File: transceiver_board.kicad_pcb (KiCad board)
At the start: 2 copper layers, 126 parts, among them J1 85505-5113, J2 Conn_01x01_Male, J3 SMA_Connector, J4 Conn_01x01_Male, J5 SMA_Connector, Q1 BC547, Q2 BC547, T1 S558-5999-46-F, U1 LAN83C185-JT, U2 ltc6752ims8-2-pbf, U4 AP63203WU, U5 AP63205WU, U6 LM317_TO-220, U7 LM317_TO-220, Y1 25 MHz

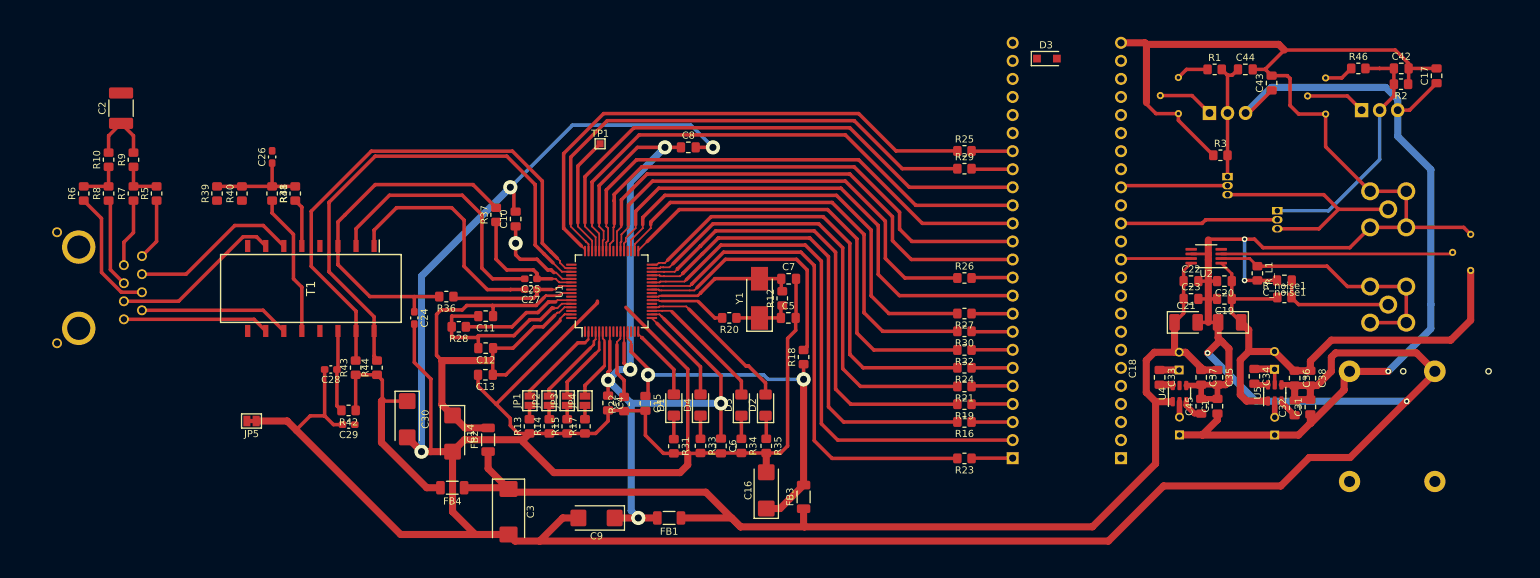
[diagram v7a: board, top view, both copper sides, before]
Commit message: tweaked power circuit, sorted drc errors and warnings, visual checked pcb
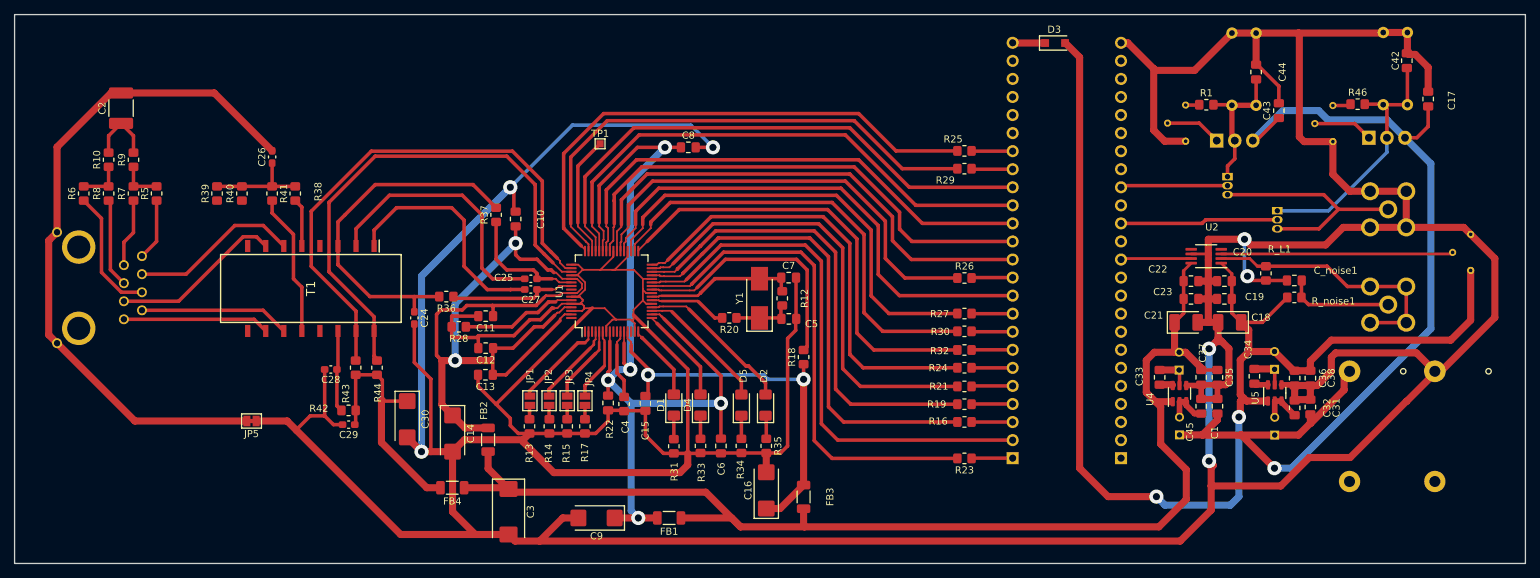
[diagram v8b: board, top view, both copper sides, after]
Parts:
- added R11: 240R, Resistor_THT:R_Axial_DIN0207_L6.3mm_D2.5mm_P10.16mm_Horizontal, B.Cu at (187.6, 43.8)
- added R4: 240R, Resistor_THT:R_Axial_DIN0207_L6.3mm_D2.5mm_P10.16mm_Horizontal, B.Cu at (212.3, 43.7)
- J3: value SMA_Connector -> Laser
- J5: value SMA_Connector -> Receiver Connector
- R1, R46: value 160 -> 180R
- R2, R3: value 120 -> 240R; footprint Resistor_SMD:R_0805_2012Metric_Pad1.20x1.40mm_HandSolder -> Resistor_THT:R_Axial_DIN0207_L6.3mm_D2.5mm_P10.16mm_Horizontal; moved to B.Cu
- moved R3 17.9 mm to (191.0, 43.8), turned to -90 degrees
- moved R2 7.69 mm to (208.9, 43.7), turned to -90 degrees
- moved R1 5.11 mm to (184.0, 53.9)
- moved R46 5.03 mm to (205.3, 53.8)
- moved C43 4.01 mm to (194.2, 54.7)
- moved RV3 4.01 mm to (181.1, 59.0)
- moved RV2 4.01 mm to (201.8, 59.1)
- moved U6 4.01 mm to (206.9, 58.5)
- moved U7 4.01 mm to (185.5, 58.9)
- moved C17 3.47 mm to (215.2, 53.1)
- moved D3 2.47 mm to (162.8, 45.2)
- moved C44 1.56 mm to (191.0, 49.3), turned to 90 degrees
- moved C_noise1 1.40 mm to (196.4, 78.6)
- moved R_noise1 1.40 mm to (196.4, 81.0)
- moved C42 1.35 mm to (212.2, 47.7), turned to 90 degrees
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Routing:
- net +5V: track 74.5 -> 175.8 mm, vias 0 -> 2
- net GND1: track 0.00 -> 96.6 mm
- net GND: track 789.4 -> 865.4 mm
- net PHY-AVDD: track 95.2 -> 119.4 mm, vias 1 -> 2
- net +12V: track 117.7 -> 135.1 mm
- net +3V3: track 164.0 -> 173.0 mm
- net Net-(D3-Pad1): track 0.00 -> 4.58 mm
- net /laser/Low volt: track 17.2 -> 20.3 mm
- net Net-(R1-Pad1): track 4.57 -> 1.93 mm
- net Net-(C33-Pad1): track 2.75 -> 4.94 mm
- net Net-(C29-Pad1): track 32.4 -> 34.4 mm
- net /laser/High volt: track 35.0 -> 37.0 mm
- net Net-(R46-Pad1): track 4.15 -> 2.56 mm
- net Net-(C_noise1-Pad1): track 16.4 -> 15.0 mm
- net Net-(C45-Pad1): track 5.07 -> 6.02 mm
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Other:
- board outline added: 212.5 x 77.2 mm
